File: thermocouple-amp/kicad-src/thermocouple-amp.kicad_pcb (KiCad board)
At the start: 2 copper layers, 36.4 x 26.7 mm, 19 parts, among them J2 Conn_01x04, U1 ADR425ARMZ, U2 AD8551RM

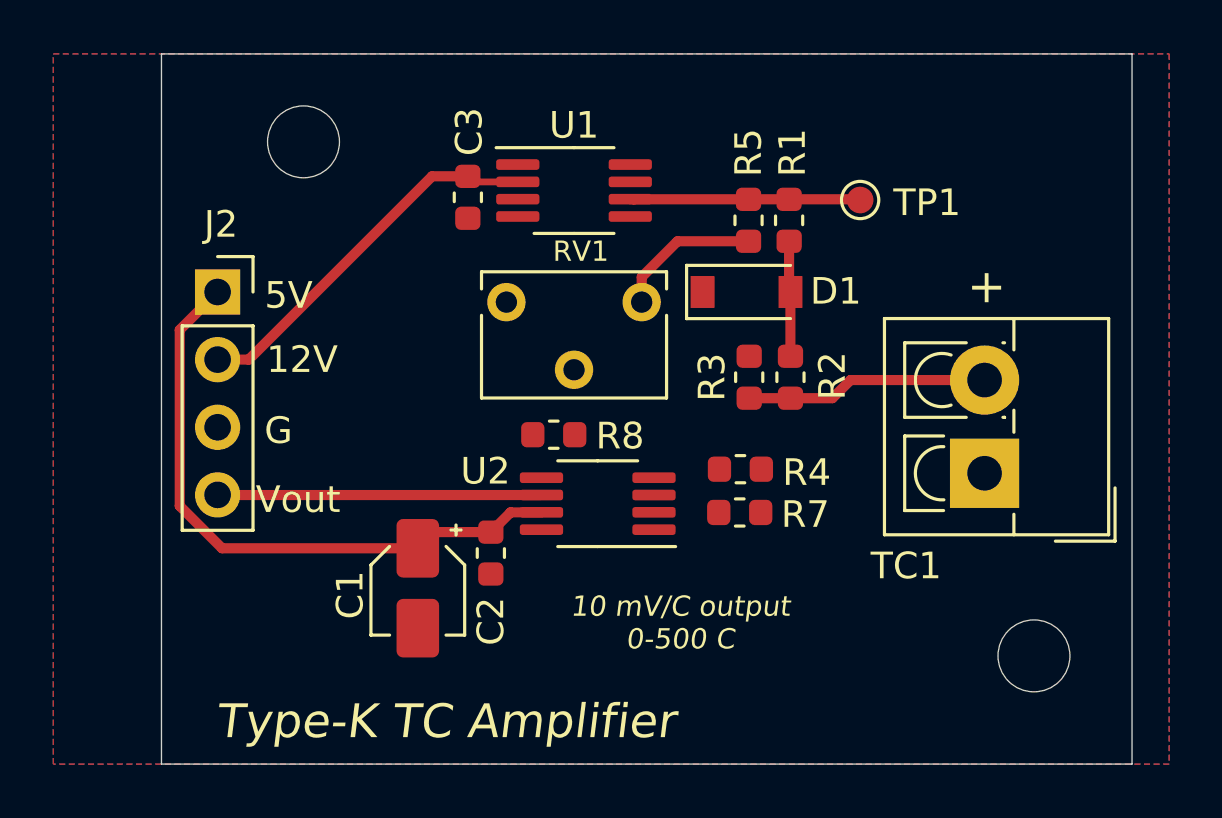
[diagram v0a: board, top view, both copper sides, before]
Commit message: adds guard trace and prod files
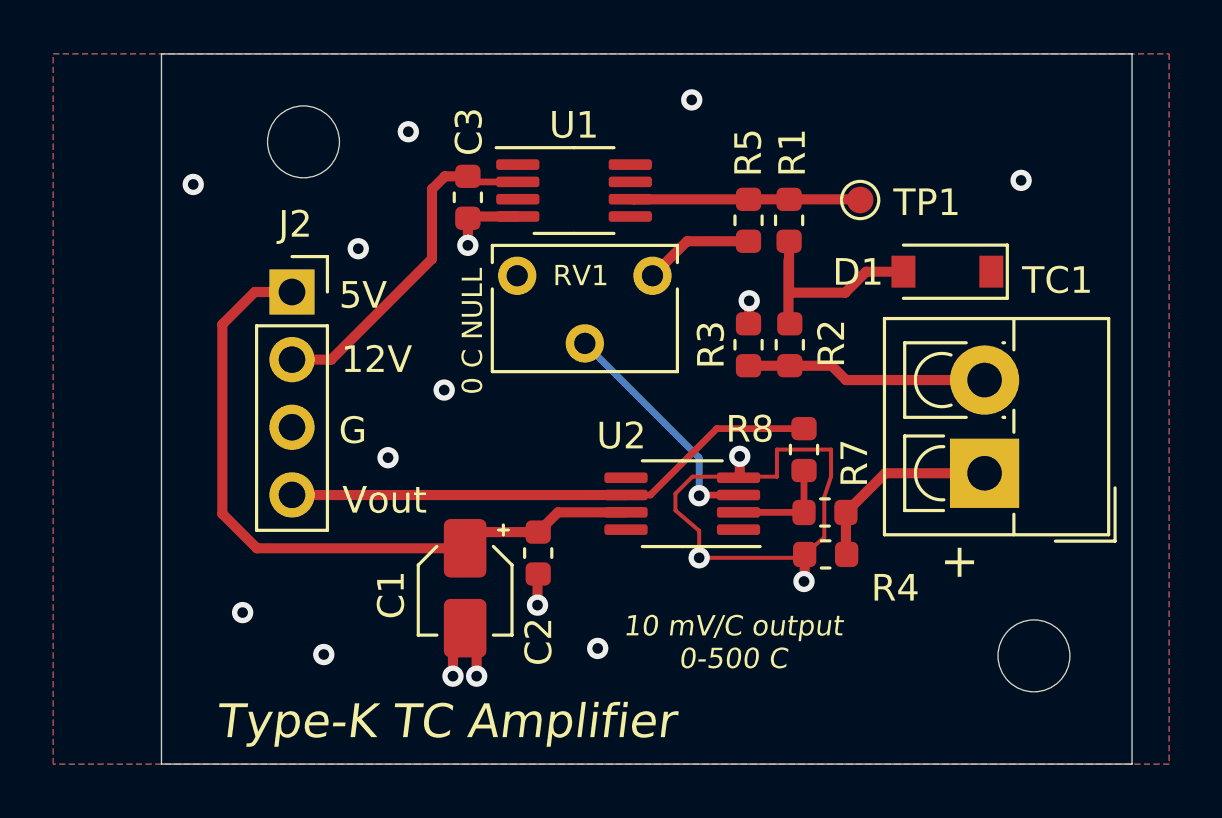
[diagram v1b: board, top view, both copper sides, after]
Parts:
- moved R8 9.41 mm to (164.1, 98.7), turned to 90 degrees
- moved D1 7.58 mm to (169.5, 92.0), turned to 180 degrees
- moved R4 4.53 mm to (164.9, 102.6)
- moved R7 3.20 mm to (164.9, 101.0)
- moved U2 3.18 mm to (159.5, 100.7)
- moved J2 2.79 mm to (144.9, 92.8)
- moved C1 1.78 mm to (151.4, 103.9)
- moved C2 1.78 mm to (154.1, 102.6)
- moved R2 1.22 mm to (163.6, 94.7)
- moved R3 1.22 mm to (162.0, 94.7)
- moved RV1 1.07 mm to (158.4, 92.2)
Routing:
- net GND: track 0.18 -> 11.0 mm, vias 0 -> 18
- net Net-(RV1-Pad2): track 0.00 -> 8.99 mm, vias 0 -> 1
- net /Vout: track 12.2 -> 20.3 mm
- net Net-(R4-Pad2): track 0.00 -> 7.40 mm
- net Net-(D1-Pad2): track 4.34 -> 8.96 mm
- net Net-(R7-Pad2): track 0.00 -> 3.68 mm
- net +5V: track 23.4 -> 26.5 mm
- net Net-(R5-Pad1): track 5.51 -> 4.14 mm
- net +12V: track 14.2 -> 12.9 mm
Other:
- board text added: "0 C NULL"

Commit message: updates tc amp gerbers
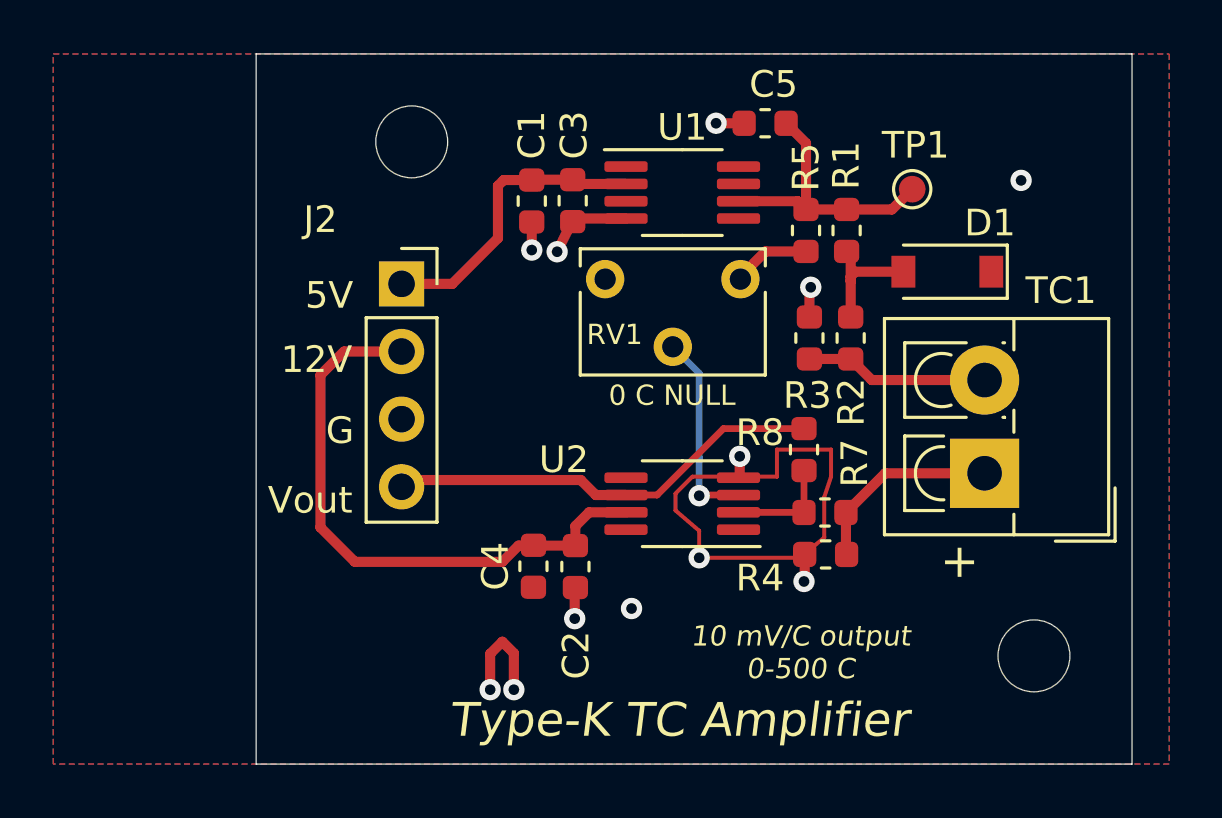
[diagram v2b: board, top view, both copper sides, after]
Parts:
- added C4: 1uF, Capacitor_SMD:C_0603_1608Metric, F.Cu at (153.9, 103.1)
- added C5: 1uF, Capacitor_SMD:C_0603_1608Metric, F.Cu at (162.6, 86.4)
- C1: value 10u -> 1uF; footprint Capacitor_SMD:CP_Elec_3x5.4 -> Capacitor_SMD:C_0603_1608Metric
- moved C1 14.8 mm to (153.9, 89.3)
- moved J2 4.13 mm to (149.0, 92.5)
- moved U1 4.06 mm to (159.5, 89.0)
- moved H1 4.06 mm to (149.4, 87.1)
- moved C3 3.94 mm to (155.4, 89.3)
- moved RV1 3.30 mm to (161.7, 92.3)
- moved R2 2.30 mm to (165.8, 94.5)
- moved R3 2.30 mm to (164.3, 94.5)
- moved R1 2.19 mm to (165.7, 90.4)
- moved R5 2.19 mm to (164.2, 90.4)
- moved TP1 2.00 mm to (168.1, 88.9)
- moved C2 1.49 mm to (155.5, 103.1)
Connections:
- net /5.000V renamed /5.00V
- C1 pad 1: +5V -> +12V
- J2 pad 1: +5V -> +12V
- J2 pad 2: +12V -> +5V
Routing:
- net +5V: track 26.5 -> 22.3 mm
- net Net-(D1-Pad2): track 8.96 -> 4.83 mm
- net /Vout: track 20.3 -> 16.9 mm
- net GND: track 11.0 -> 13.6 mm, vias 18 -> 12
- net Net-(R2-Pad1): track 9.09 -> 6.91 mm
- net /5.00V: track 8.64 -> 10.5 mm
- net Net-(RV1-Pad2): track 8.99 -> 7.57 mm
- net +12V: track 12.9 -> 11.6 mm
- net Net-(R5-Pad1): track 4.14 -> 2.95 mm
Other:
- board size 36.4 x 26.7 mm -> 32.9 x 26.7 mm
